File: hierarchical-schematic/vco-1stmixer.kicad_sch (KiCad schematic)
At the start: 44 parts, among them J101 VCO Control In, J102 1st IF Out, J103 VCO Sample, J104 RF In, J105 Conn_01x02, U101 POS-200, U102 MAV-11, U103 MAV-11, U104 TUF-1H+

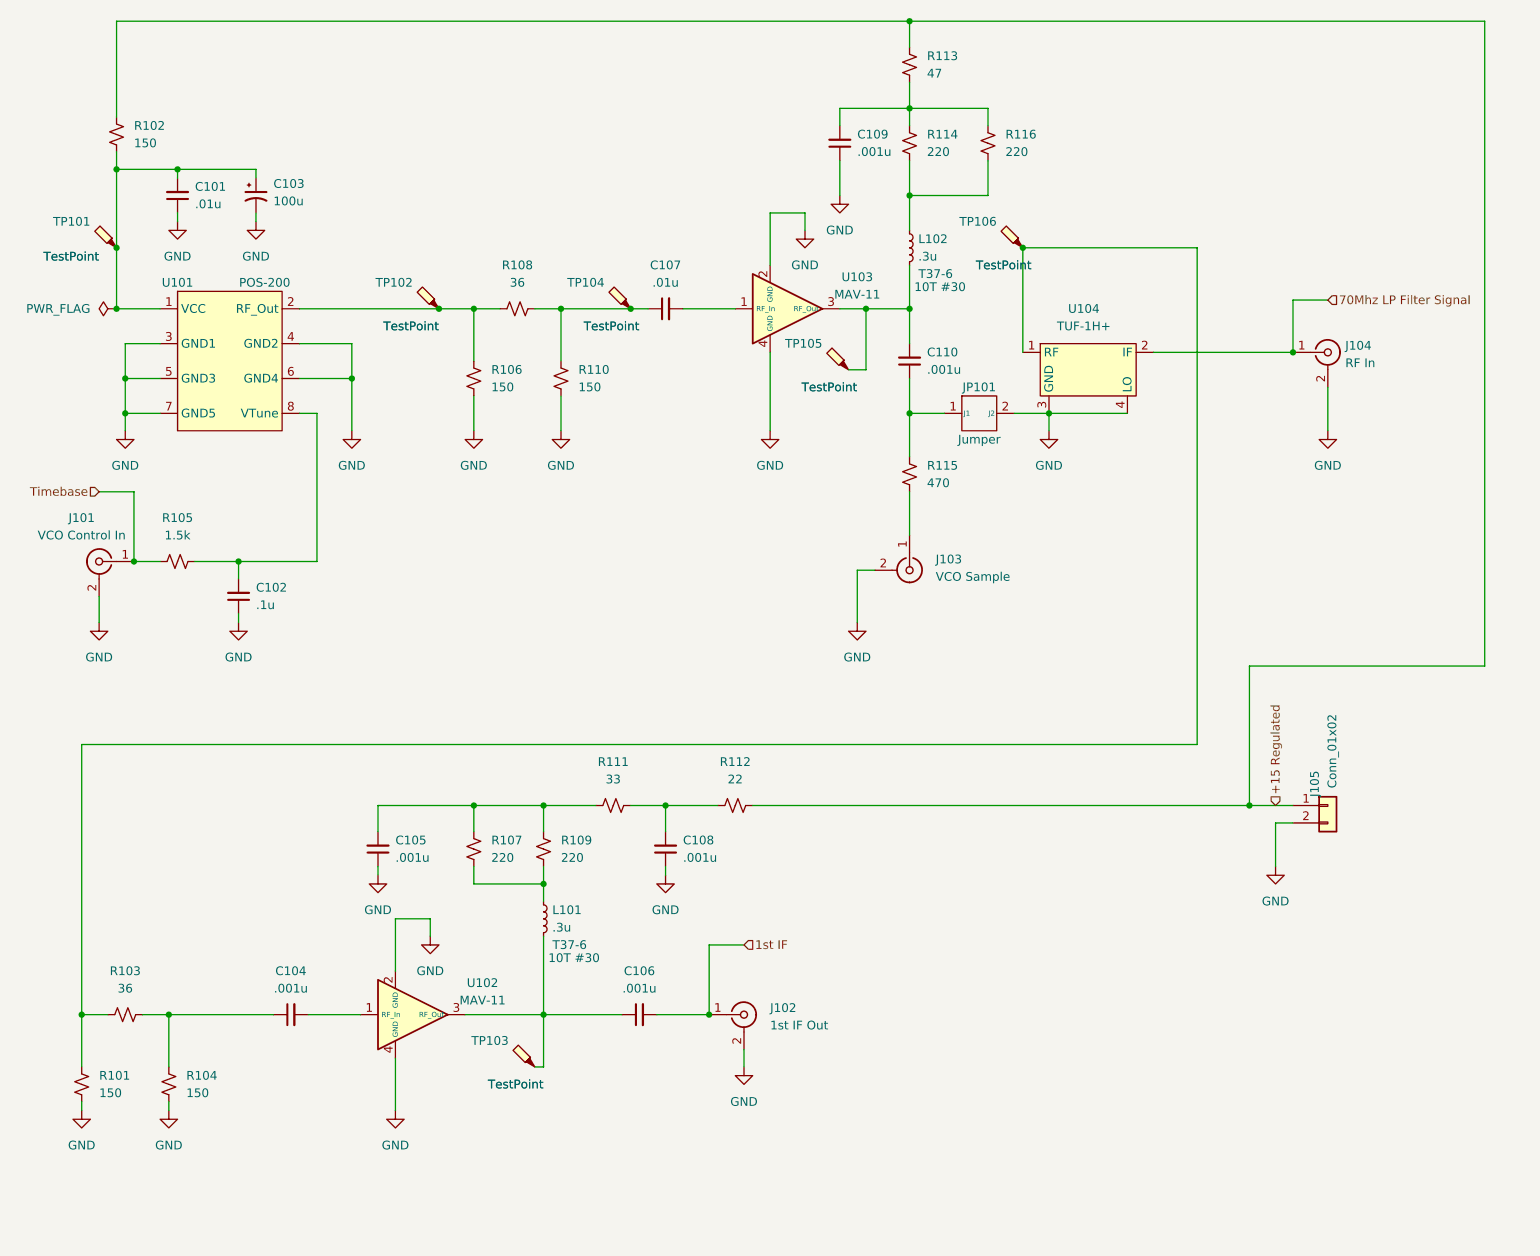
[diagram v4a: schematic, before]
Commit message: erc changes for hierarchical schematic
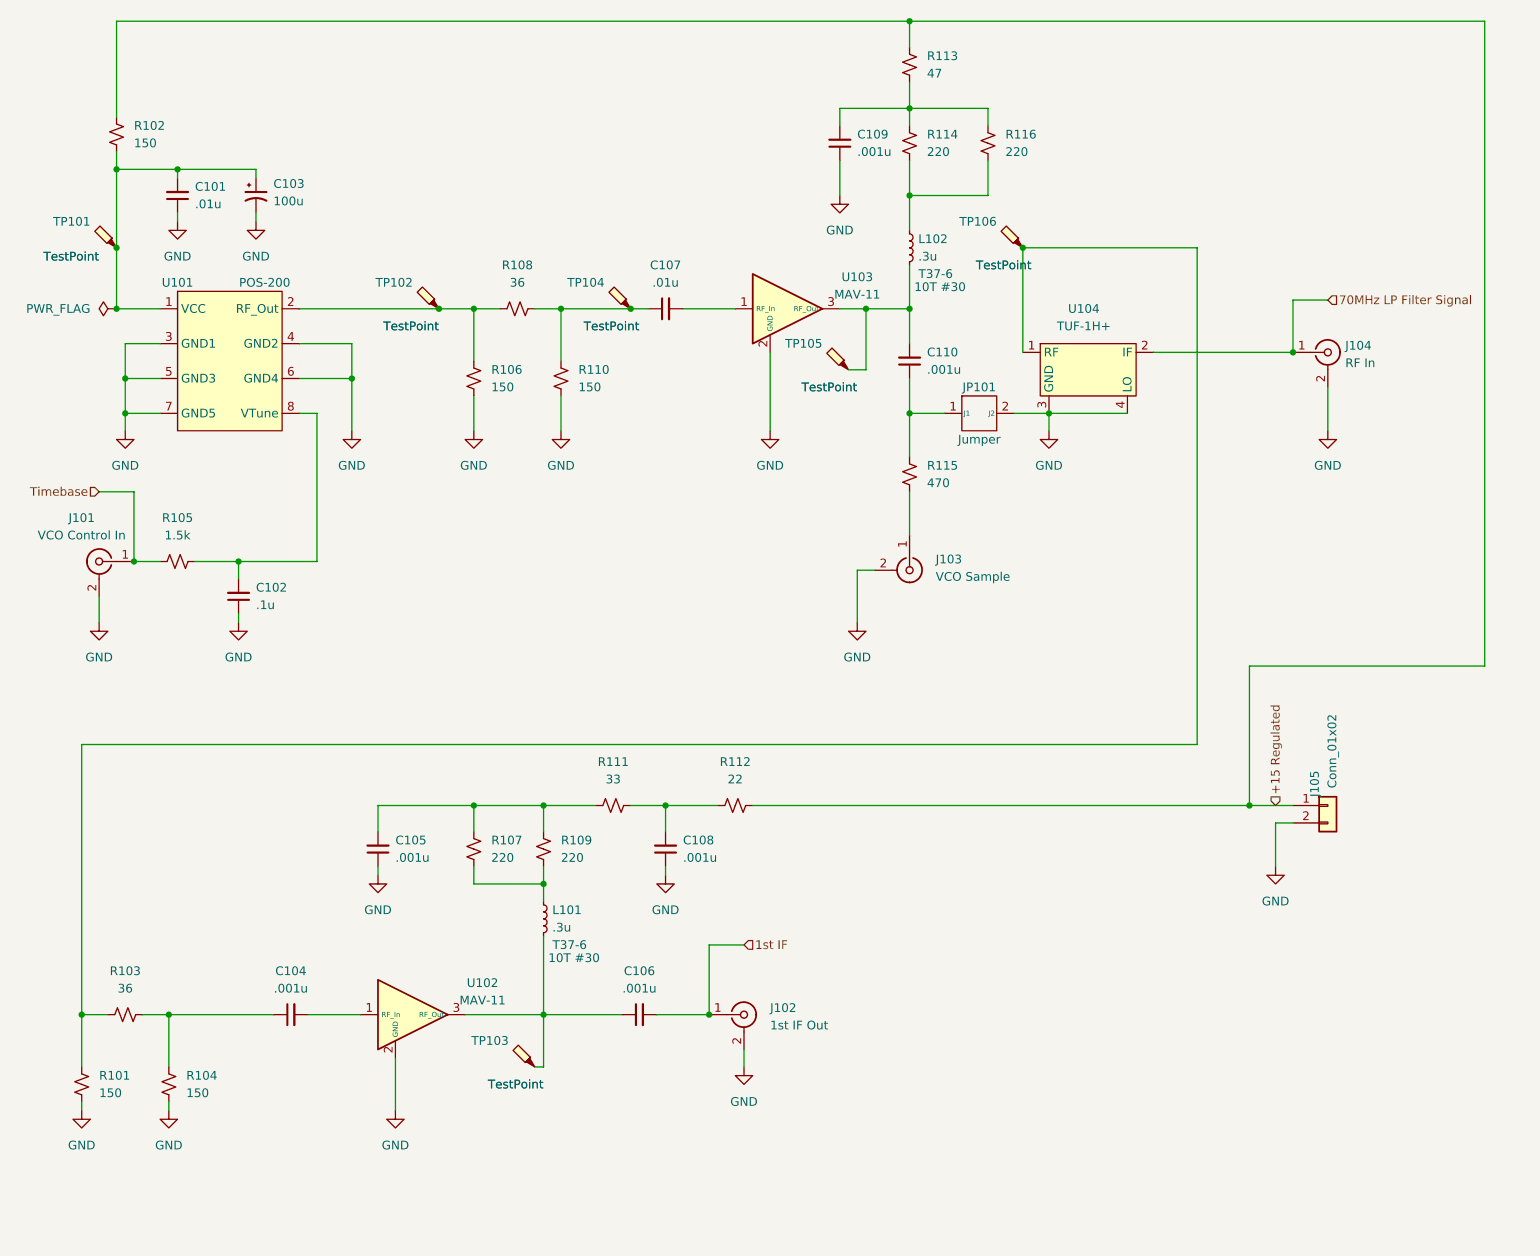
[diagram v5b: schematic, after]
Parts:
- U102, U103: footprint vco-1stmixer:MAV-11BSM&plus_ -> spectrum_analyzer:MAV-11BSM&plus_
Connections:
- net 70Mhz LP Filter Signal renamed 70MHz LP Filter Signal
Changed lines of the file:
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@@
-    (stroke (width 0) (type default))
-  )
-  (wire (pts (xy 127 161.29) (xy 127 153.67))
     (stroke (width 0) (type default))
   )
@@
     (stroke (width 0) (type default))
   )
-  (wire (pts (xy 127 153.67) (xy 132.08 153.67))
-    (stroke (width 0) (type default))
-  )
   (wire (pts (xy 148.59 151.13) (xy 148.59 148.59))
     (stroke (width 0) (type default))
@@
     (stroke (width 0) (type default))
   )
-  (wire (pts (xy 132.08 153.67) (xy 132.08 156.21))
-    (stroke (width 0) (type default))
-  )
   (wire (pts (xy 87.63 80.01) (xy 87.63 82.55))
     (stroke (width 0) (type default))
   )
-  (wire (pts (xy 181.61 58.42) (xy 181.61 50.8))
-    (stroke (width 0) (type default))
-  )
   (wire (pts (xy 124.46 140.97) (xy 124.46 137.16))
     (stroke (width 0) (type default))
   )
-  (wire (pts (xy 186.69 50.8) (xy 186.69 53.34))
-    (stroke (width 0) (type default))
-  )
   (wire (pts (xy 81.28 167.64) (xy 85.09 167.64))
-    (stroke (width 0) (type default))
-  )
-  (wire (pts (xy 181.61 50.8) (xy 186.69 50.8))
     (stroke (width 0) (type default))
   )
@@
     (effects (font (size 1.27 1.27)) (justify left))
   )
-  (hierarchical_label "70Mhz LP Filter Signal" (shape input) (at 262.89 63.5 0) (fields_autoplaced)
+  (hierarchical_label "70MHz LP Filter Signal" (shape input) (at 262.89 63.5 0) (fields_autoplaced)
     (effects (font (size 1.27 1.27)) (justify left))
   )
@@
       (effects (font (size 1.27 1.27)) hide)
     )
+    (property "Sim.Enable" "0" (at 227.33 73.66 0)
+      (effects (font (size 1.27 1.27)) hide)
+    )
     (pin "1")
     (pin "2")
@@
     )
   )
-  (symbol (lib_id "power:GND") (at 186.69 53.34 0) (unit 1)
-    (in_bom yes) (on_board yes) (dnp no) (fields_autoplaced)
-    (property "Reference" "#PWR0117" (at 186.69 59.69 0)
-      (effects (font (size 1.27 1.27)) hide)
-    )
-    (property "Value" "GND" (at 186.69 58.42 0)
-      (effects (font (size 1.27 1.27)))
-    )
-    (property "Footprint" "" (at 186.69 53.34 0)
-      (effects (font (size 1.27 1.27)) hide)
-    )
-    (property "Datasheet" "" (at 186.69 53.34 0)
-      (effects (font (size 1.27 1.27)) hide)
-    )
-    (pin "1")
-    (instances
-      (project "W7ZOI Spectrum Analyzer"
-        (path "/d5173421-a214-4849-aa93-f108d8644c8a/cdcab9f9-dac7-455c-a5f6-cabc856b606c"
-          (reference "#PWR0117") (unit 1)
-        )
-      )
-    )
-  )
   (symbol (lib_id "Connector:TestPoint_Probe") (at 161.29 64.77 90) (unit 1)
     (in_bom yes) (on_board yes) (dnp no)
@@
     )
   )
-  (symbol (lib_id "power:GND") (at 132.08 156.21 0) (unit 1)
-    (in_bom yes) (on_board yes) (dnp no) (fields_autoplaced)
-    (property "Reference" "#PWR0111" (at 132.08 162.56 0)
-      (effects (font (size 1.27 1.27)) hide)
-    )
-    (property "Value" "GND" (at 132.08 161.29 0)
-      (effects (font (size 1.27 1.27)))
-    )
-    (property "Footprint" "" (at 132.08 156.21 0)
-      (effects (font (size 1.27 1.27)) hide)
-    )
-    (property "Datasheet" "" (at 132.08 156.21 0)
-      (effects (font (size 1.27 1.27)) hide)
-    )
-    (pin "1")
-    (instances
-      (project "W7ZOI Spectrum Analyzer"
-        (path "/d5173421-a214-4849-aa93-f108d8644c8a/cdcab9f9-dac7-455c-a5f6-cabc856b606c"
-          (reference "#PWR0111") (unit 1)
-        )
-      )
-    )
-  )
   (symbol (lib_id "Connector:Conn_Coaxial") (at 83.82 101.6 0) (mirror y) (unit 1)
     (in_bom yes) (on_board yes) (dnp no)
@@
       (effects (font (size 1.27 1.27)) hide)
     )
+    (property "Sim.Enable" "0" (at 83.82 101.6 0)
+      (effects (font (size 1.27 1.27)) hide)
+    )
     (pin "1")
     (pin "2")
@@
       (effects (font (size 1.27 1.27)))
     )
-    (property "Footprint" "vco-1stmixer:MAV-11BSM&plus_" (at 181.61 64.77 0)
-      (effects (font (size 1.27 1.27)) hide)
-    )
-    (property "Datasheet" "https://www.minicircuits.com/pdfs/MAV-11+.pdf" (at 181.61 64.77 0)
+    (property "Footprint" "spectrum_analyzer:MAV-11BSM&plus_" (at 181.61 64.77 0)
+      (effects (font (size 1.27 1.27)) hide)
+    )
+    (property "Datasheet" "https://www.minicircuits.com/pdfs/MAV-11BSM+.pdf" (at 181.61 64.77 0)
       (effects (font (size 1.27 1.27)) hide)
     )
@@
     )
   )
-  (symbol (lib_id "spectrum analyzer:MAV-11") (at 127 167.64 0) (unit 1)
+  (symbol (lib_name "MAV-11_1") (lib_id "spectrum analyzer:MAV-11") (at 127 167.64 0) (unit 1)
     (in_bom yes) (on_board yes) (dnp no) (fields_autoplaced)
     (property "Reference" "U102" (at 139.7 163.0233 0)
@@
       (effects (font (size 1.27 1.27)))
     )
-    (property "Footprint" "vco-1stmixer:MAV-11BSM&plus_" (at 127 167.64 0)
-      (effects (font (size 1.27 1.27)) hide)
-    )
-    (property "Datasheet" "https://www.minicircuits.com/pdfs/MAV-11+.pdf" (at 127 167.64 0)
+    (property "Footprint" "spectrum_analyzer:MAV-11BSM&plus_" (at 127 167.64 0)
+      (effects (font (size 1.27 1.27)) hide)
+    )
+    (property "Datasheet" "https://www.minicircuits.com/pdfs/MAV-11BSM+.pdf" (at 127 167.64 0)
       (effects (font (size 1.27 1.27)) hide)
     )
@@
     )
     (property "Datasheet" " ~" (at 201.93 102.87 0)
+      (effects (font (size 1.27 1.27)) hide)
+    )
+    (property "Sim.Enable" "0" (at 201.93 102.87 0)
       (effects (font (size 1.27 1.27)) hide)
     )
@@
       (effects (font (size 1.27 1.27)) hide)
     )
+    (property "Sim.Enable" "0" (at 177.8 167.64 0)
+      (effects (font (size 1.27 1.27)) hide)
+    )
